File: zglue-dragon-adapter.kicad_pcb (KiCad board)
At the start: 6 copper layers, 25 x 20 mm, 59 parts, among them J1 543630489, J2 543630489, U1 zGlue-Dragon

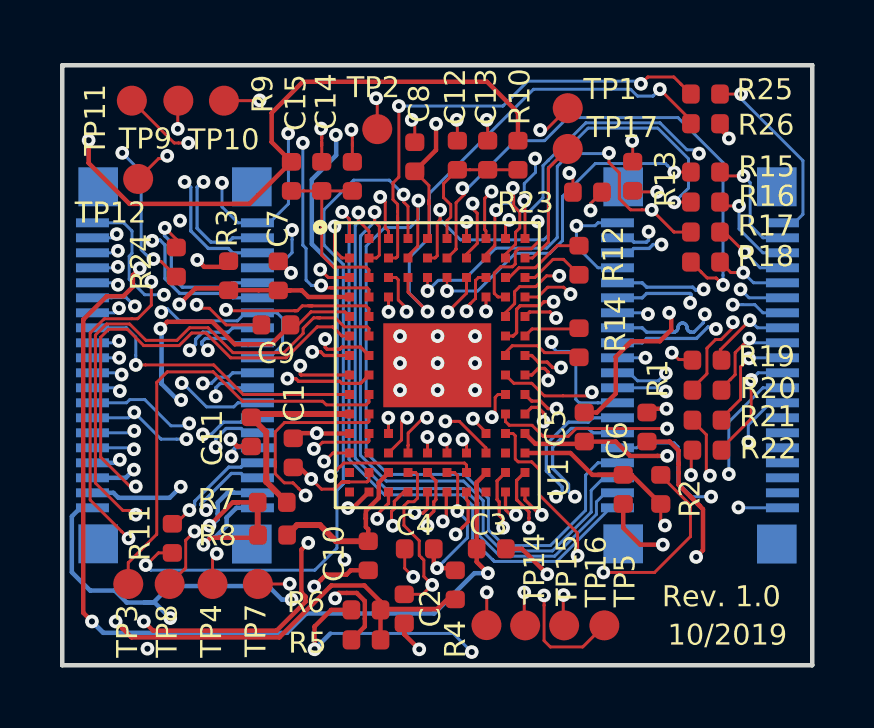
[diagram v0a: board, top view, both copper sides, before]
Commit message: Modified LGA-96 thermal pad on paste layer
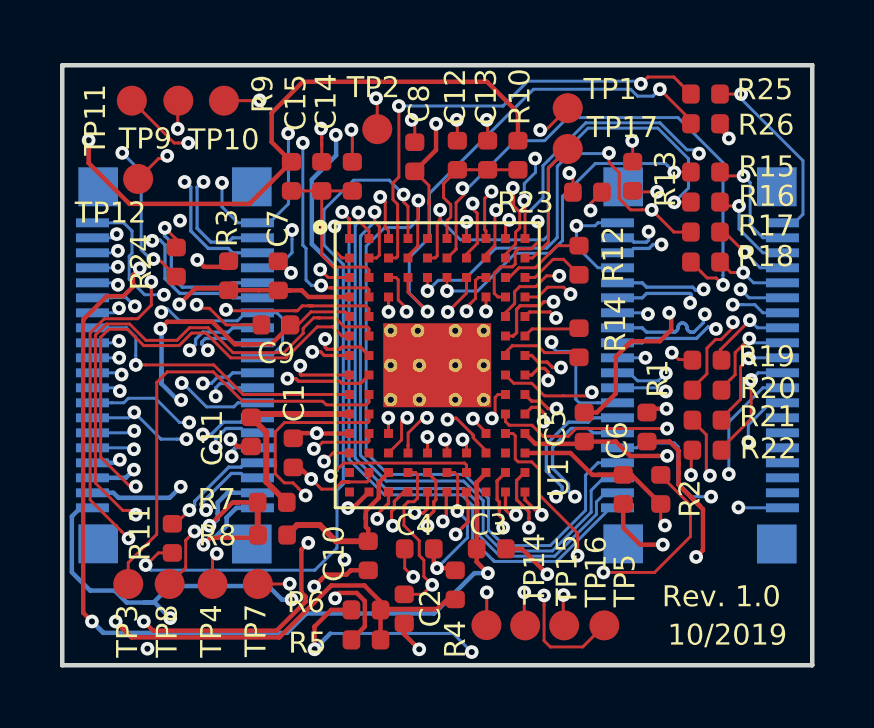
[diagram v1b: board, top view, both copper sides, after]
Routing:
- net /I2C_0_SCL: track 15.2 -> 16.6 mm
- net GND: vias 43 -> 34
